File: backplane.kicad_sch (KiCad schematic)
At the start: 2 parts, among them J1 09031967921, U1 TPD2E2U06DCK

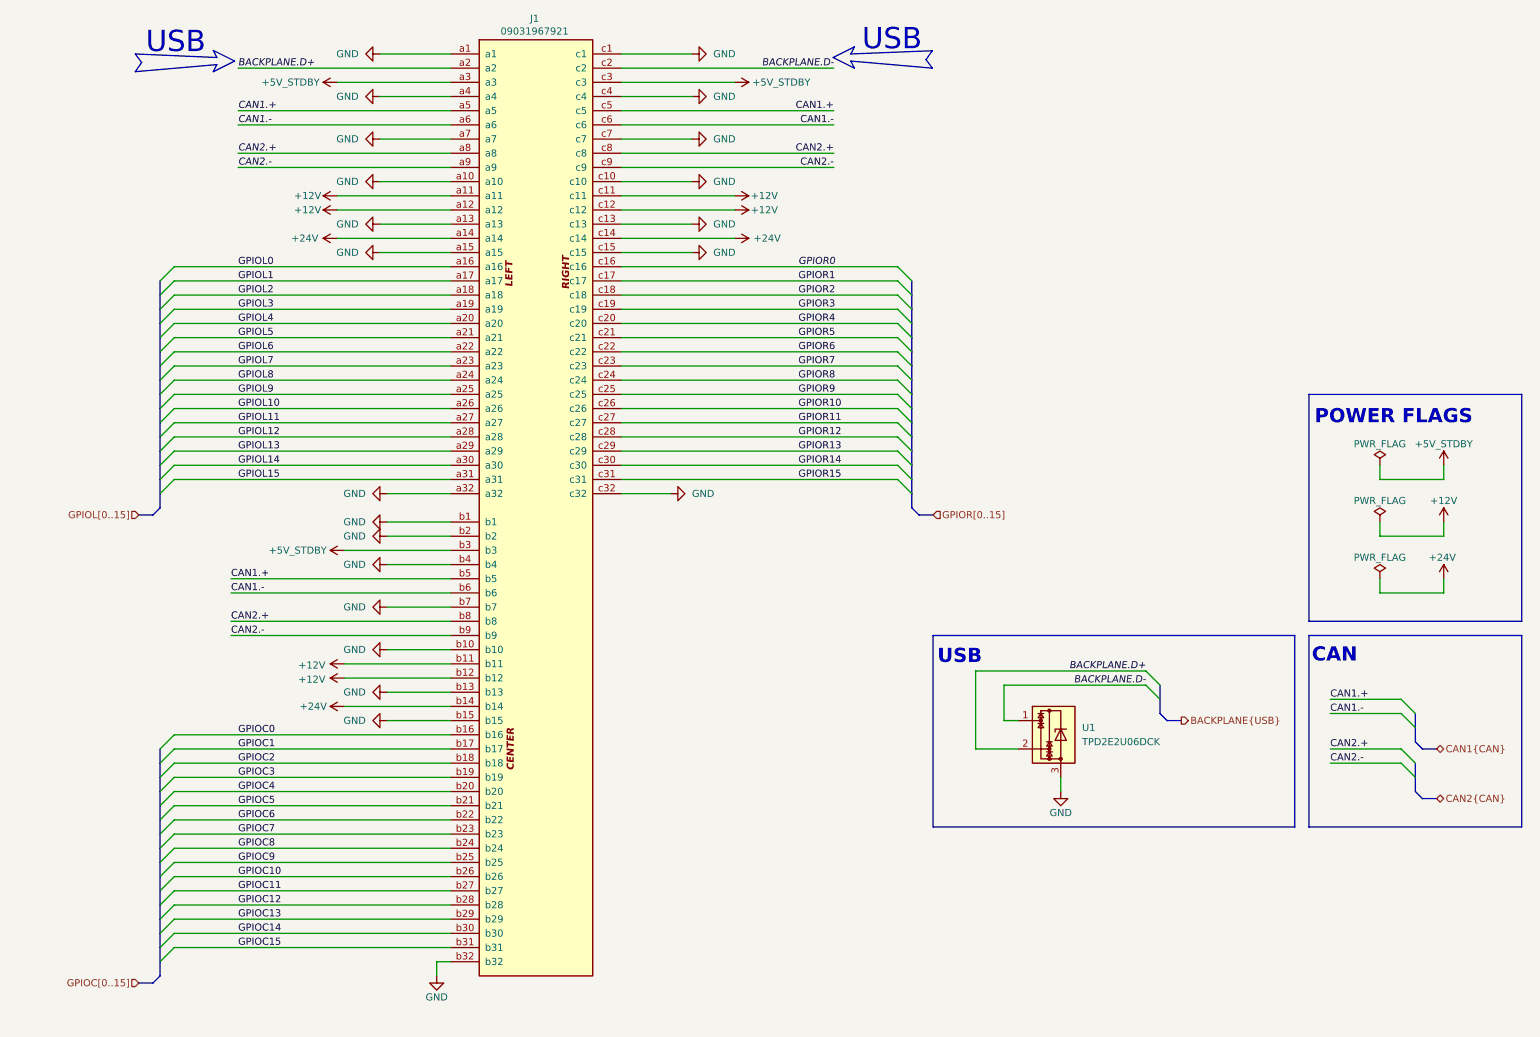
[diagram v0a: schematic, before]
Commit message: [#1] WIP: Change components to ones from the global library, refactor schematic
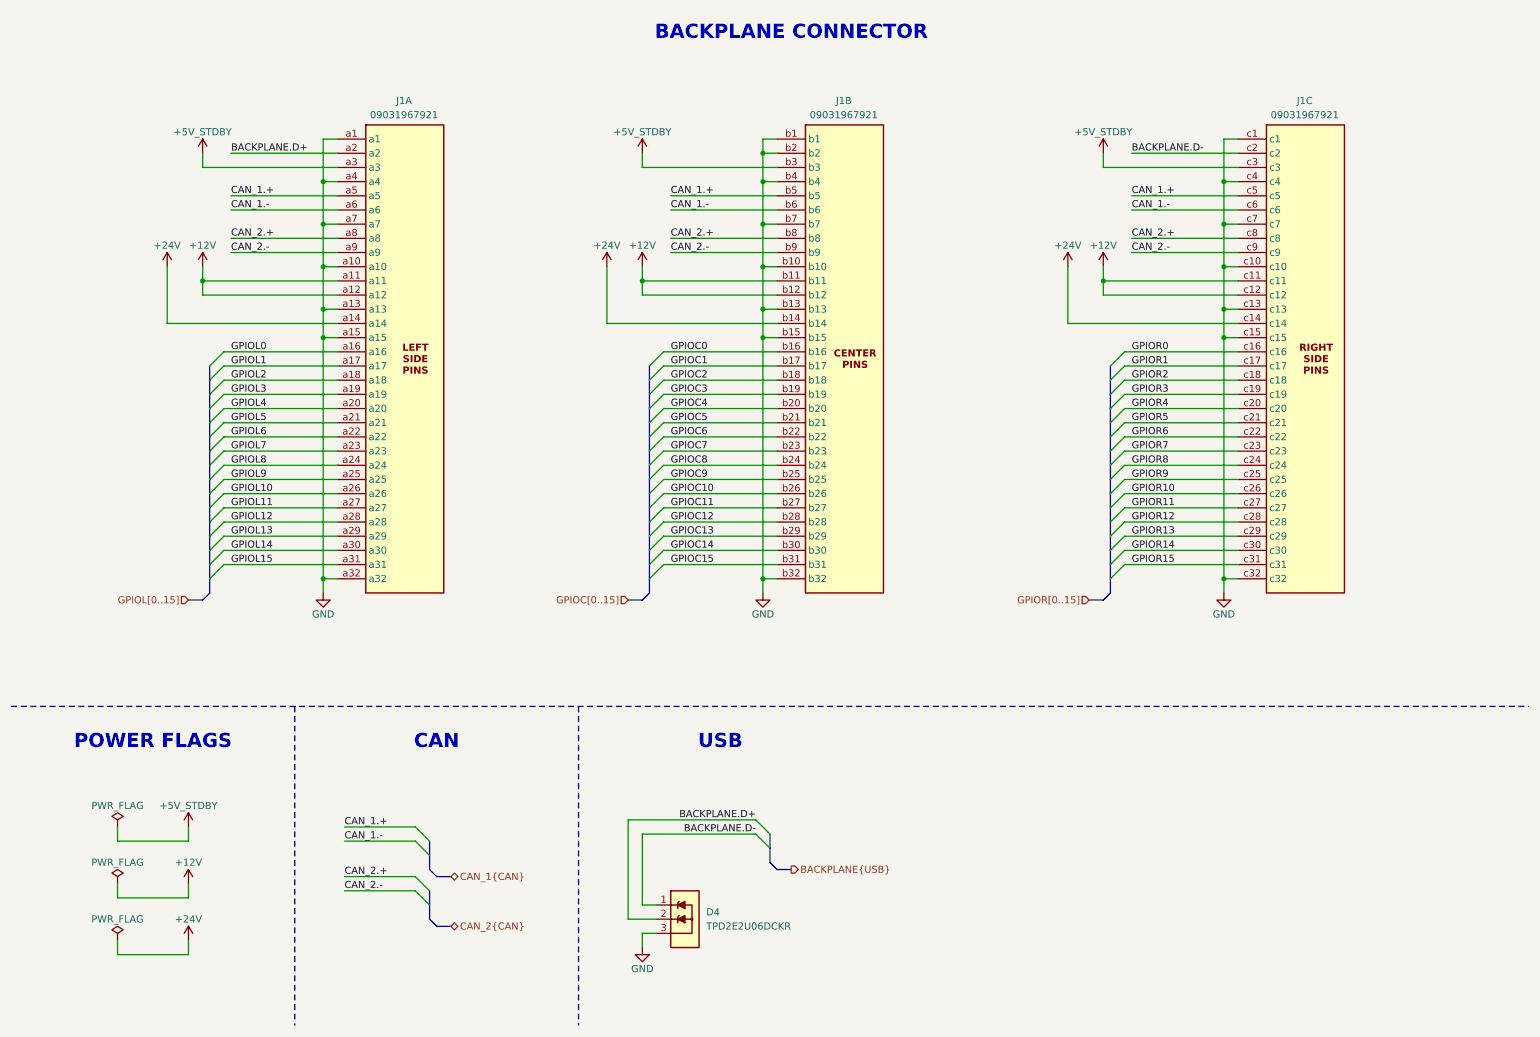
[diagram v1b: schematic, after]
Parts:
- removed J1: 09031967921, Connector_DIN:DIN41612_R_3x32_Female_Horizontal_THT, symbol DIN41612_3x32:09031967921
- removed U1: TPD2E2U06DCK, Package_TO_SOT_SMD:SOT-323_SC-70, symbol Power_Protection:TPD2E2U06DCK
- added D4: TPD2E2U06DCKR, DW-footprints:SOT-323, symbol DW-TVS:TPD2E2U06DCKR
- added J1: DIN-41612-connector_09031967921, DW-footprints:Conn_DIN_41612_09031967921, symbol DW-connectors:DIN-41612_09031967921
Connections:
- net +12V: now also J1.a11, J1.a12, J1.b11, J1.b12, J1.c11, J1.c12
- net +24V: now also J1.a14, J1.b14, J1.c14
- net +5V_STDBY: now also J1.a3, J1.b3, J1.c3
- net BACKPLANE.D+: now also D4.2, J1.a2
- net BACKPLANE.D-: now also D4.1, J1.c2
- net GND: now also D4.3, J1.a1, J1.a10, J1.a13, J1.a15, J1.a32, J1.a4, J1.a7, J1.b1, J1.b10, J1.b13, J1.b15, J1.b2, J1.b32, J1.b4, J1.b7, J1.c1, J1.c10, J1.c13, J1.c15, J1.c32, J1.c4, J1.c7
- net GPIOC0: now also J1.b16
- net GPIOC1: now also J1.b17
- net GPIOC10: now also J1.b26
- net GPIOC11: now also J1.b27
- net GPIOC12: now also J1.b28
- net GPIOC13: now also J1.b29
- net GPIOC14: now also J1.b30
- net GPIOC15: now also J1.b31
- net GPIOC2: now also J1.b18
- net GPIOC3: now also J1.b19
- net GPIOC4: now also J1.b20
- net GPIOC5: now also J1.b21
- net GPIOC6: now also J1.b22
- net GPIOC7: now also J1.b23
- net GPIOC8: now also J1.b24
- net GPIOC9: now also J1.b25
- net GPIOL0: now also J1.a16
- net GPIOL1: now also J1.a17
- net GPIOL10: now also J1.a26
- net GPIOL11: now also J1.a27
- net GPIOL12: now also J1.a28
- net GPIOL13: now also J1.a29
- net GPIOL14: now also J1.a30
- net GPIOL15: now also J1.a31
- net GPIOL2: now also J1.a18
- net GPIOL3: now also J1.a19
- net GPIOL4: now also J1.a20
- net GPIOL5: now also J1.a21
- net GPIOL6: now also J1.a22
- net GPIOL7: now also J1.a23
- net GPIOL8: now also J1.a24
- net GPIOL9: now also J1.a25
- net GPIOR0: now also J1.c16
- net GPIOR1: now also J1.c17
- net GPIOR10: now also J1.c26
- net GPIOR11: now also J1.c27
- net GPIOR12: now also J1.c28
- net GPIOR13: now also J1.c29
- net GPIOR14: now also J1.c30
- net GPIOR15: now also J1.c31
- net GPIOR2: now also J1.c18
- net GPIOR3: now also J1.c19
- net GPIOR4: now also J1.c20
- net GPIOR5: now also J1.c21
- net GPIOR6: now also J1.c22
- net GPIOR7: now also J1.c23
- net GPIOR8: now also J1.c24
- net GPIOR9: now also J1.c25
- new net CAN_1.+: J1.a5, J1.b5, J1.c5
- new net CAN_1.-: J1.a6, J1.b6, J1.c6
- new net CAN_2.+: J1.a8, J1.b8, J1.c8
- new net CAN_2.-: J1.a9, J1.b9, J1.c9
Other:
- note added: "BACKPLANE CONNECTOR"

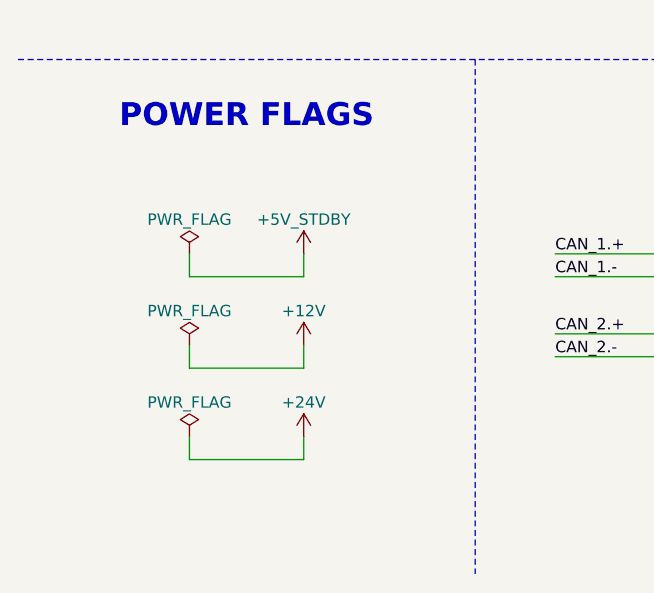
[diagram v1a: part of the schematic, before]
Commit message: [#1] Change components to ones from the global library, add debug console, refactor schematic
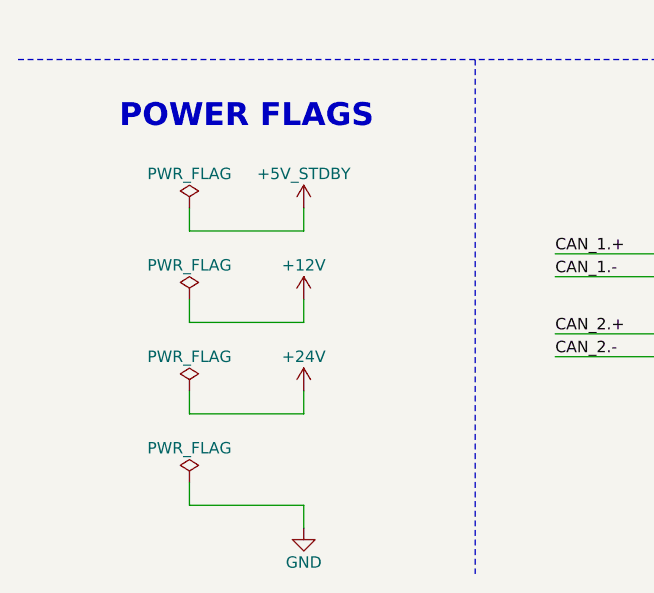
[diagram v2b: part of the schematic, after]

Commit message: [#1] Re-annotate schematic
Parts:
- renumbered D4 to D1
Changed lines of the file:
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@@
+		(polyline
+			(pts
+				(xy 69.85 181.61) (xy 111.76 181.61) (xy 111.76 156.21) (xy 69.85 156.21)
+			)
+			(stroke
+				(width 0)
+				(type dash)
+			)
+			(fill
+				(type none)
+			)
+		)
+	)
+	(rule_area
 		(polyline
 			(pts
 				(xy 120.65 171.45) (xy 171.45 171.45) (xy 171.45 156.21) (xy 120.65 156.21)
-			)
-			(stroke
-				(width 0)
-				(type dash)
-			)
-			(fill
-				(type none)
-			)
-		)
-	)
-	(rule_area
-		(polyline
-			(pts
-				(xy 69.85 181.61) (xy 111.76 181.61) (xy 111.76 156.21) (xy 69.85 156.21)
 			)
 			(stroke
@@
 		(on_board yes)
 		(dnp no)
-		(property "Reference" "#PWR06"
+		(property "Reference" "#PWR02"
 			(at 125.73 44.45 0)
 			(effects
@@
 			(project "cm5-module"
 				(path "/090a8e41-87a8-4fb1-998b-60a2c0dc4cee/ff3476d7-2f10-4f79-9864-988601c7ce1b"
-					(reference "#PWR06")
+					(reference "#PWR02")
 					(unit 1)
 				)
@@
 		(on_board yes)
 		(dnp no)
-		(property "Reference" "#PWR033"
+		(property "Reference" "#PWR04"
 			(at 40.64 64.77 0)
 			(effects
@@
 			(project ""
 				(path "/090a8e41-87a8-4fb1-998b-60a2c0dc4cee/ff3476d7-2f10-4f79-9864-988601c7ce1b"
-					(reference "#PWR033")
+					(reference "#PWR04")
 					(unit 1)
 				)
@@
 		(on_board yes)
 		(dnp no)
-		(property "Reference" "#PWR041"
+		(property "Reference" "#PWR017"
 			(at 44.45 198.12 0)
 			(effects
@@
 			(project "cm5-module"
 				(path "/090a8e41-87a8-4fb1-998b-60a2c0dc4cee/ff3476d7-2f10-4f79-9864-988601c7ce1b"
-					(reference "#PWR041")
+					(reference "#PWR017")
 					(unit 1)
 				)
@@
 		(on_board yes)
 		(dnp no)
-		(property "Reference" "#PWR057"
+		(property "Reference" "#PWR013"
 			(at 44.45 160.02 0)
 			(effects
@@
 			(project "cm5-module"
 				(path "/090a8e41-87a8-4fb1-998b-60a2c0dc4cee/ff3476d7-2f10-4f79-9864-988601c7ce1b"
-					(reference "#PWR057")
+					(reference "#PWR013")
 					(unit 1)
 				)
@@
 		(on_board yes)
 		(dnp no)
-		(property "Reference" "#PWR036"
+		(property "Reference" "#PWR06"
 			(at 119.38 64.77 0)
 			(effects
@@
 			(project "cm5-module"
 				(path "/090a8e41-87a8-4fb1-998b-60a2c0dc4cee/ff3476d7-2f10-4f79-9864-988601c7ce1b"
-					(reference "#PWR036")
+					(reference "#PWR06")
 					(unit 1)
 				)
@@
 		(on_board yes)
 		(dnp no)
-		(property "Reference" "#FLG07"
+		(property "Reference" "#FLG01"
 			(at 31.75 154.305 0)
 			(effects
@@
 			(project "cm5-module"
 				(path "/090a8e41-87a8-4fb1-998b-60a2c0dc4cee/ff3476d7-2f10-4f79-9864-988601c7ce1b"
-					(reference "#FLG07")
+					(reference "#FLG01")
 					(unit 1)
 				)
@@
 		(on_board yes)
 		(dnp no)
-		(property "Reference" "#PWR010"
+		(property "Reference" "#PWR012"
 			(at 229.87 125.73 0)
 			(effects
@@
 			(project "cm5-module"
 				(path "/090a8e41-87a8-4fb1-998b-60a2c0dc4cee/ff3476d7-2f10-4f79-9864-988601c7ce1b"
-					(reference "#PWR010")
+					(reference "#PWR012")
 					(unit 1)
 				)
@@
 		(on_board yes)
 		(dnp no)
-		(property "Reference" "#PWR01"
+		(property "Reference" "#PWR016"
 			(at 125.73 189.23 0)
 			(effects
@@
 			(project ""
 				(path "/090a8e41-87a8-4fb1-998b-60a2c0dc4cee/ff3476d7-2f10-4f79-9864-988601c7ce1b"
-					(reference "#PWR01")
+					(reference "#PWR016")
 					(unit 1)
 				)
@@
 		(on_board yes)
 		(dnp no)
-		(property "Reference" "#FLG06"
+		(property "Reference" "#FLG02"
 			(at 31.75 164.465 0)
 			(effects
@@
 			(project "cm5-module"
 				(path "/090a8e41-87a8-4fb1-998b-60a2c0dc4cee/ff3476d7-2f10-4f79-9864-988601c7ce1b"
-					(reference "#FLG06")
+					(reference "#FLG02")
 					(unit 1)
 				)
@@
 		(on_board yes)
 		(dnp no)
-		(property "Reference" "#PWR04"
+		(property "Reference" "#PWR05"
 			(at 46.99 64.77 0)
 			(effects
@@
 			(project ""
 				(path "/090a8e41-87a8-4fb1-998b-60a2c0dc4cee/ff3476d7-2f10-4f79-9864-988601c7ce1b"
-					(reference "#PWR04")
+					(reference "#PWR05")
 					(unit 1)
 				)
@@
 		(on_board yes)
 		(dnp no)
-		(property "Reference" "#FLG05"
+		(property "Reference" "#FLG04"
 			(at 31.75 184.785 0)
 			(effects
@@
 			(project "cm5-module"
 				(path "/090a8e41-87a8-4fb1-998b-60a2c0dc4cee/ff3476d7-2f10-4f79-9864-988601c7ce1b"
-					(reference "#FLG05")
+					(reference "#FLG04")
 					(unit 1)
 				)
@@
 		(dnp no)
 		(fields_autoplaced yes)
-		(property "Reference" "D4"
+		(property "Reference" "D1"
 			(at 137.16 176.53 0)
 			(effects
@@
 			(project ""
 				(path "/090a8e41-87a8-4fb1-998b-60a2c0dc4cee/ff3476d7-2f10-4f79-9864-988601c7ce1b"
-					(reference "D4")
+					(reference "D1")
 					(unit 1)
 				)
@@
 		(on_board yes)
 		(dnp no)
-		(property "Reference" "#PWR037"
+		(property "Reference" "#PWR08"
 			(at 201.93 64.77 0)
 			(effects
@@
 			(project "cm5-module"
 				(path "/090a8e41-87a8-4fb1-998b-60a2c0dc4cee/ff3476d7-2f10-4f79-9864-988601c7ce1b"
-					(reference "#PWR037")
+					(reference "#PWR08")
 					(unit 1)
 				)
@@
 		(on_board yes)
 		(dnp no)
-		(property "Reference" "#PWR061"
+		(property "Reference" "#PWR014"
 			(at 44.45 170.18 0)
 			(effects
@@
 			(project "cm5-module"
 				(path "/090a8e41-87a8-4fb1-998b-60a2c0dc4cee/ff3476d7-2f10-4f79-9864-988601c7ce1b"
-					(reference "#PWR061")
+					(reference "#PWR014")
 					(unit 1)
 				)
@@
 		(on_board yes)
 		(dnp no)
-		(property "Reference" "#PWR08"
+		(property "Reference" "#PWR03"
 			(at 208.28 44.45 0)
 			(effects
@@
 			(project "cm5-module"
 				(path "/090a8e41-87a8-4fb1-998b-60a2c0dc4cee/ff3476d7-2f10-4f79-9864-988601c7ce1b"
-					(reference "#PWR08")
+					(reference "#PWR03")
 					(unit 1)
 				)
@@
 		(on_board yes)
 		(dnp no)
-		(property "Reference" "#PWR05"
+		(property "Reference" "#PWR01"
 			(at 46.99 44.45 0)
 			(effects
@@
 			(project ""
 				(path "/090a8e41-87a8-4fb1-998b-60a2c0dc4cee/ff3476d7-2f10-4f79-9864-988601c7ce1b"
-					(reference "#PWR05")
+					(reference "#PWR01")
 					(unit 1)
 				)
@@
 		(on_board yes)
 		(dnp no)
-		(property "Reference" "#PWR038"
+		(property "Reference" "#PWR015"
 			(at 44.45 180.34 0)
 			(effects
@@
 			(project "cm5-module"
 				(path "/090a8e41-87a8-4fb1-998b-60a2c0dc4cee/ff3476d7-2f10-4f79-9864-988601c7ce1b"
-					(reference "#PWR038")
+					(reference "#PWR015")
 					(unit 1)
 				)
@@
 		(on_board yes)
 		(dnp no)
-		(property "Reference" "#PWR02"
+		(property "Reference" "#PWR010"
 			(at 68.58 125.73 0)
 			(effects
@@
 			(project "cm5-module"
 				(path "/090a8e41-87a8-4fb1-998b-60a2c0dc4cee/ff3476d7-2f10-4f79-9864-988601c7ce1b"
-					(reference "#PWR02")
+					(reference "#PWR010")
 					(unit 1)
 				)
@@
 		(on_board yes)
 		(dnp no)
-		(property "Reference" "#PWR03"
+		(property "Reference" "#PWR011"
 			(at 147.32 125.73 0)
 			(effects
@@
 			(project "cm5-module"
 				(path "/090a8e41-87a8-4fb1-998b-60a2c0dc4cee/ff3476d7-2f10-4f79-9864-988601c7ce1b"
-					(reference "#PWR03")
+					(reference "#PWR011")
 					(unit 1)
 				)
@@
 		(on_board yes)
 		(dnp no)
-		(property "Reference" "#FLG04"
+		(property "Reference" "#FLG03"
 			(at 31.75 174.625 0)
 			(effects
@@
 			(project ""
 				(path "/090a8e41-87a8-4fb1-998b-60a2c0dc4cee/ff3476d7-2f10-4f79-9864-988601c7ce1b"
-					(reference "#FLG04")
+					(reference "#FLG03")
 					(unit 1)
 				)
